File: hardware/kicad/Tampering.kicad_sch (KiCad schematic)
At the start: 0 parts

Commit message: finished schematics
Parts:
- added C50: 100nF, symbol Device:C
- added JP1: Jumper, Package_TO_SOT_SMD:SOT-23-5_HandSoldering, symbol Jumper:SolderJumper_2_Open
- added R36: 10KΩ, symbol Device:R
- added S4: TSA017A2518B, TSA017A2518B:TSA017A2518B, symbol dk_Tactile-Switches:B3F-1000
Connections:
- new net +STM_3V3: R36.1
- new net GND: C50.2, JP1.1 (A), S4.3, S4.4
- new net TAMPER: C50.1, JP1.2 (B), R36.2, S4.1, S4.2

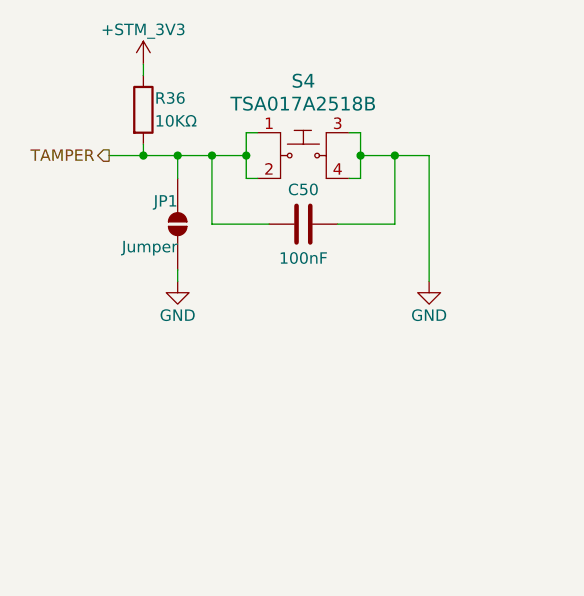
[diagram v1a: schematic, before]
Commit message: schematics refinement
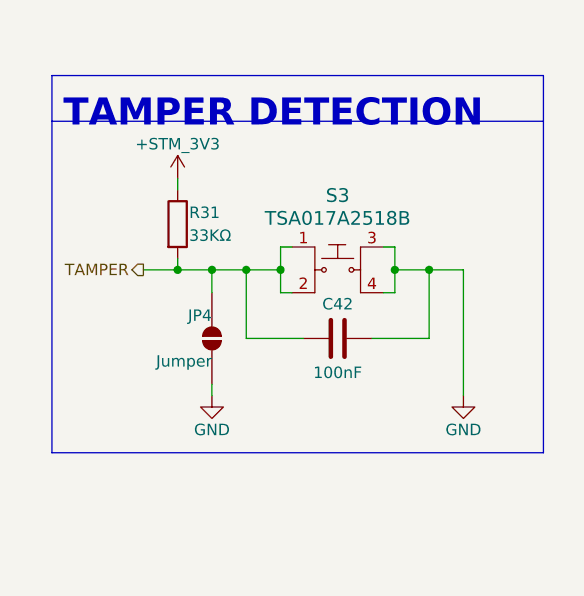
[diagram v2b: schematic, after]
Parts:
- C42: renamed from C50; footprint (none) -> Capacitor_SMD:C_0603_1608Metric_Pad1.08x0.95mm_HandSolder
- JP4: renamed from JP1; footprint Package_TO_SOT_SMD:SOT-23-5_HandSoldering -> Jumper:SolderJumper-2_P1.3mm_Open_RoundedPad1.0x1.5mm
- R31: renamed from R36; value 10KΩ -> 33KΩ; footprint (none) -> Resistor_SMD:R_0805_2012Metric_Pad1.20x1.40mm_HandSolder
- renumbered S4 to S3
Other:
- note added: "TAMPER DETECTION"
- moved on the sheet: C42, JP4, R31, S3

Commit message: started PCB and changed power system
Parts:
- renumbered C42 to C39, R31 to R22
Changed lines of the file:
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@@
 		(in_pos_files yes)
 		(dnp no)
-		(property "Reference" "R31"
+		(property "Reference" "R22"
 			(at 88.9 46.99 0)
 			(show_name no)
@@
 			(project "crypto_node"
 				(path "/6c72b0cb-17b9-42a6-811c-297d0c354af3/e87e5251-6a6f-477d-99f2-f9bb3f6c7b88"
-					(reference "R31")
+					(reference "R22")
 					(unit 1)
 				)
@@
 		(in_pos_files yes)
 		(dnp no)
-		(property "Reference" "#PWR096"
+		(property "Reference" "#PWR086"
 			(at 91.44 73.66 0)
 			(hide yes)
@@
 			(project "crypto_node"
 				(path "/6c72b0cb-17b9-42a6-811c-297d0c354af3/e87e5251-6a6f-477d-99f2-f9bb3f6c7b88"
-					(reference "#PWR096")
+					(reference "#PWR086")
 					(unit 1)
 				)
@@
 		(in_pos_files yes)
 		(dnp no)
-		(property "Reference" "C42"
+		(property "Reference" "C39"
 			(at 105.41 57.15 90)
 			(show_name no)
@@
 			(project "crypto_node"
 				(path "/6c72b0cb-17b9-42a6-811c-297d0c354af3/e87e5251-6a6f-477d-99f2-f9bb3f6c7b88"
-					(reference "C42")
+					(reference "C39")
 					(unit 1)
 				)
@@
 		(in_pos_files yes)
 		(dnp no)
-		(property "Reference" "#PWR095"
+		(property "Reference" "#PWR085"
 			(at 87.63 46.99 0)
 			(hide yes)
@@
 			(project "crypto_node"
 				(path "/6c72b0cb-17b9-42a6-811c-297d0c354af3/e87e5251-6a6f-477d-99f2-f9bb3f6c7b88"
-					(reference "#PWR095")
+					(reference "#PWR085")
 					(unit 1)
 				)
@@
 		(in_pos_files yes)
 		(dnp no)
-		(property "Reference" "#PWR097"
+		(property "Reference" "#PWR087"
 			(at 119.38 73.66 0)
 			(hide yes)
@@
 			(project "crypto_node"
 				(path "/6c72b0cb-17b9-42a6-811c-297d0c354af3/e87e5251-6a6f-477d-99f2-f9bb3f6c7b88"
-					(reference "#PWR097")
+					(reference "#PWR087")
 					(unit 1)
 				)

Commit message: Final hardware cleanup push (hopefully)
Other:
- company: (none) -> Done By :- Arudhran
- title: (none) -> Cryptographic Tactical Node
- moved on the sheet: C39, JP4, R22, S3
